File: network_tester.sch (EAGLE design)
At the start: 47 parts, among them SW1 SPST_TACT-KMR2, U1 Joystick, U2 RN2483, U3 ATSAMD21G-A, U5 MCP1640, X1 GPS, X2 868, X3 32.768, X4 microUSB, X5 434

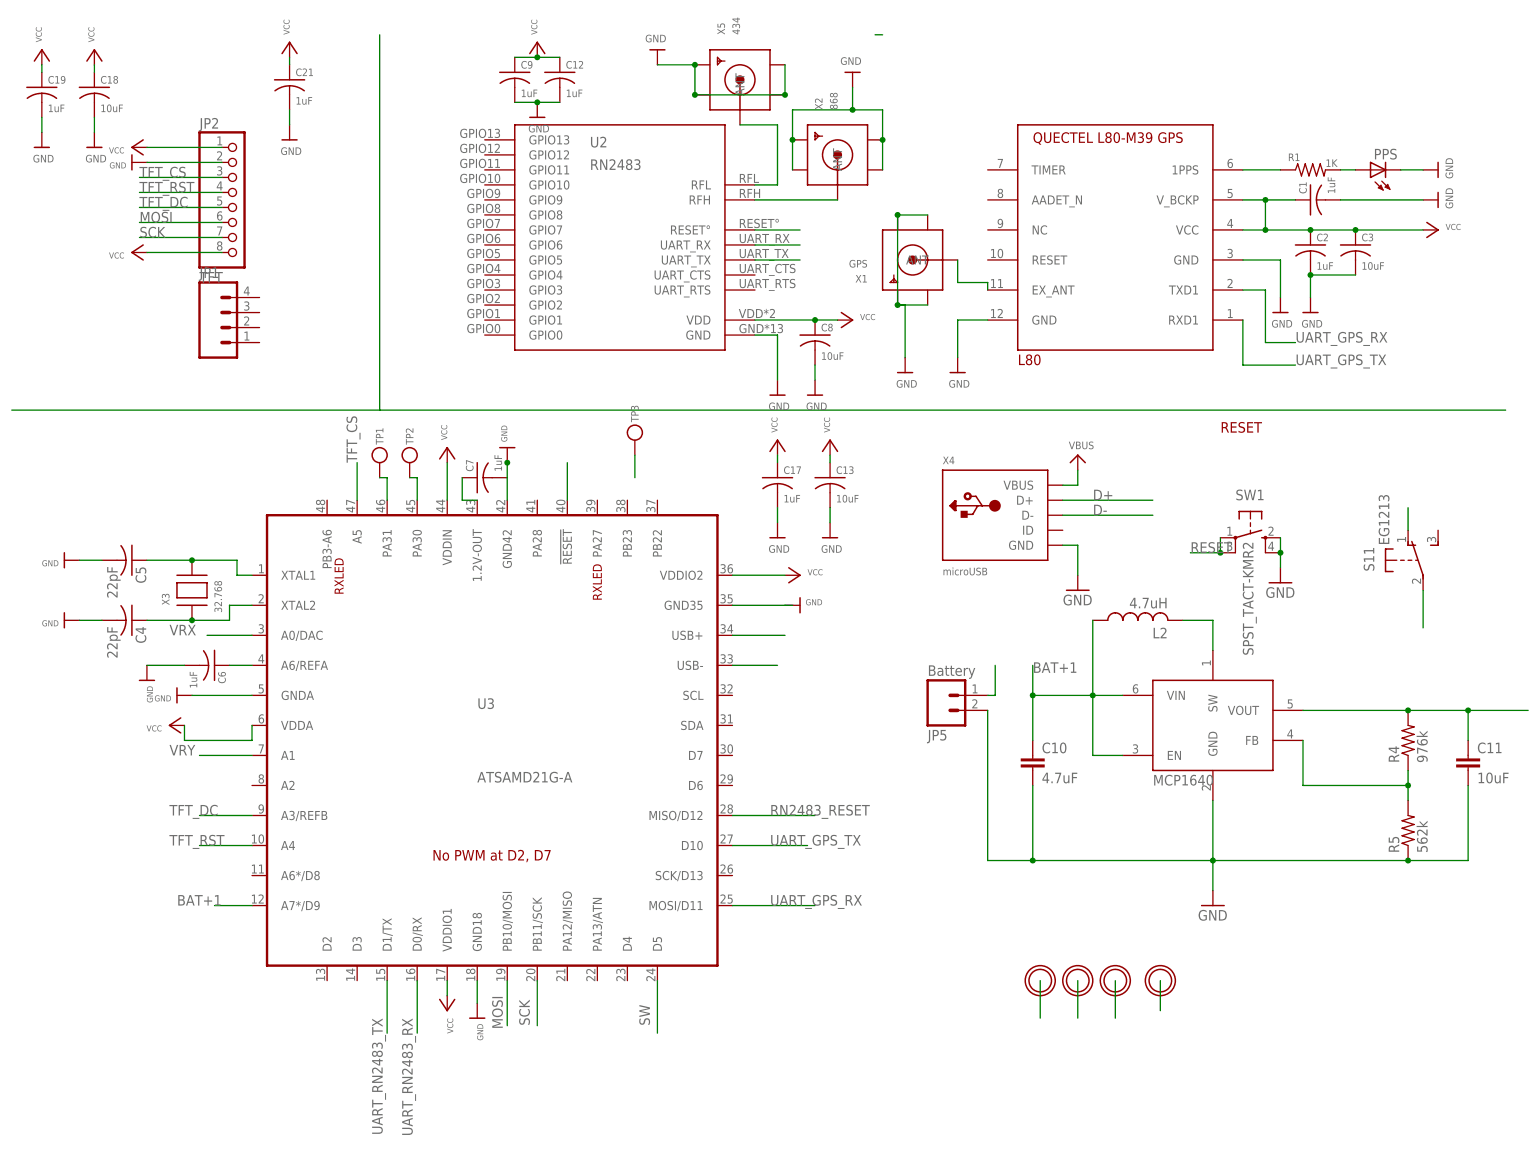
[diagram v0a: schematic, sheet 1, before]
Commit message: Test points added, fixed board labels
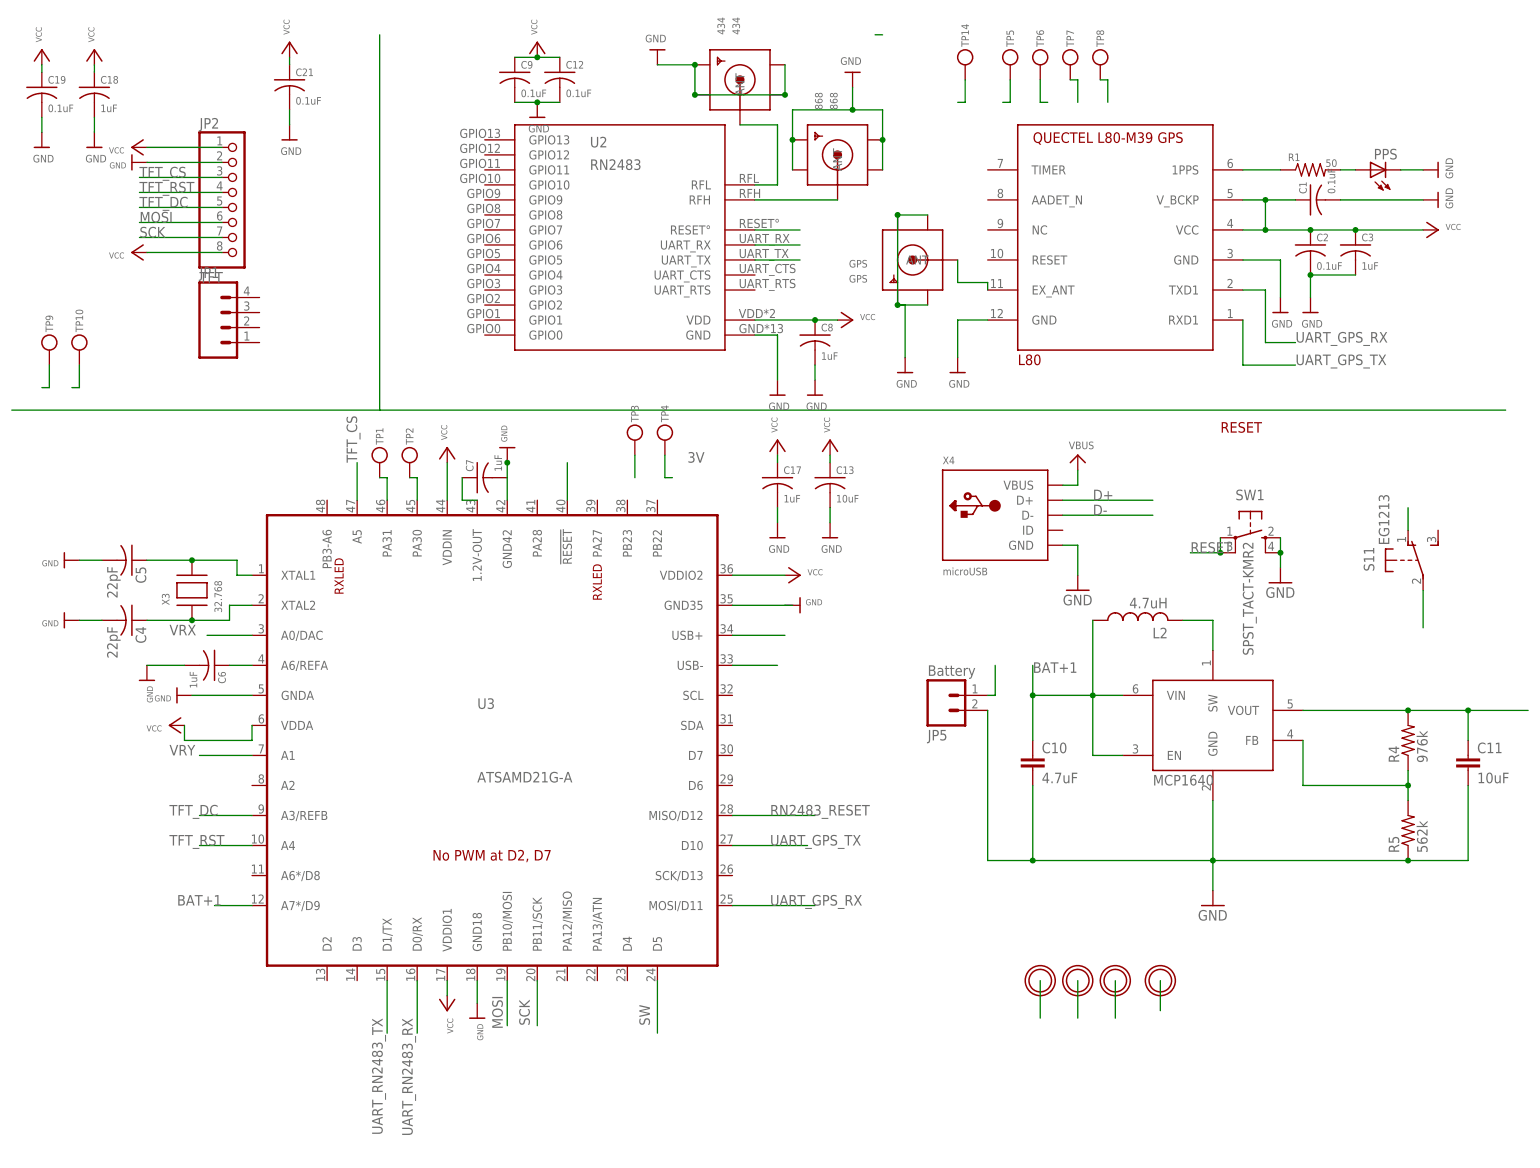
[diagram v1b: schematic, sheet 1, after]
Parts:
- added TP10, TP14, TP4, TP5, TP6, TP7, TP8, TP9: (no value), Adafruit Feather M0 Basic rev C:TESTPOINTROUND1.5MM
- C1, C12, C14, C15, C19, C2, C21, C9: value 1uF -> 0.1uF
- C16, C18, C3, C8: value 10uF -> 1uF
- R1: value 1K -> 50
- renumbered X1 to GPS, X2 to 868, X5 to 434
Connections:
- net 3V: now also TP4.P$1
- net MOSI: now also TP9.P$1
- net RN2483_RESET: now also TP14.P$1
- net SCK: now also TP10.P$1
- net UART_GPS_RX: now also TP7.P$1
- net UART_GPS_TX: now also TP8.P$1
- net UART_RN2483_RX: now also TP6.P$1
- net UART_RN2483_TX: now also TP5.P$1

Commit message: test point resolved
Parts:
- removed TP10, TP14, TP5, TP6, TP7, TP8, TP9: (no value), Adafruit Feather M0 Basic rev C:TESTPOINTROUND1.5MM
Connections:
- net MOSI: no longer TP9.P$1
- net RN2483_RESET: no longer TP14.P$1
- net SCK: no longer TP10.P$1
- net UART_GPS_RX: no longer TP7.P$1
- net UART_GPS_TX: no longer TP8.P$1
- net UART_RN2483_RX: no longer TP6.P$1
- net UART_RN2483_TX: no longer TP5.P$1

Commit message: First commit of board for external fabbing -- untested
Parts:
- removed PPS: (no value), adafruit:LEDCHIPLED_0805
- removed SW1: SPST_TACT-KMR2, adafruit:SPST_TACT-KMR2
- removed X3: 32.768, Adafruit Feather M0 Basic rev C:XTAL-3.2X1.5
- added C20, C22, C23: 100nf, Seeed-Capacitor:CERAMIC-100NF-25V-10%-X7R(0402)
- added D1: RED-0805, Seeed-LED:SMD-LED-CLEAR-RED(0805)
- added SW2: DHT-4235A, Seeed-Switch:SMD-BUTTON-TOP-DHT-4235A(4P-4.2X3.2MM)
- added Y1: 32.768, Seeed-Crystal Oscillator:SMD-CRYSTAL-32.768KHZ-12.5PF-20PPM-90K(2P-L2.0X1.2MM)
- C1, C12, C14, C15, C19, C2, C21, C9: value 0.1uF -> 100nf; device adafruit:C-USC0603 -> Seeed-Capacitor:CERAMIC-100NF-25V-10%-X7R(0402)
- C10: value 4.7uF -> 4.7uf; device SparkFun:CAP0805 -> Seeed-Capacitor:CERAMIC-4.7UF-6.3V-20%-X5R(0402)
- C11: value 10uF -> 10uf; device SparkFun:CAP0805 -> Seeed-Capacitor:CERAMIC-10UF-6.3V-20%-X5R(0402)
- C13: value 10uF -> 10uf; device adafruit:C-USC0805 -> Seeed-Capacitor:CERAMIC-10UF-6.3V-20%-X5R(0402)
- C16: value 1uF -> 1UF; device adafruit:C-USC0805 -> Seeed-Capacitor:CERAMIC-1UF-6.3V-10%-X5R(0402)
- C17, C7: value 1uF -> 1UF; device adafruit:C-USC0603 -> Seeed-Capacitor:CERAMIC-1UF-6.3V-10%-X5R(0402)
- C18, C3, C8: value 1uF -> 1UF 6.3V; device adafruit:C-USC0805 -> Seeed-Capacitor:CERAMIC-1UF-6.3V-10%-X5R(0402)
- C4, C5: value 22pF -> 22pf; device adafruit:C-USC0603 -> Seeed-Capacitor:CERAMIC-22PF-50V-5%-NPO(0402)
- C6: value 1uF -> 1UF 6.3V; device adafruit:C-USC0603 -> Seeed-Capacitor:CERAMIC-1UF-6.3V-10%-X5R(0402)
- U3: value ATSAMD21G-A -> ATSAMD21G-M; device Albert-Arduino:ATSAMD21G-A -> Albert-Arduino:ATSAMD21G-M
- X4: value microUSB -> ZX62-B-5PA; device microbuilder:USB_MICRO_20329_V2 -> Seeed-Connector:MICRO-USB-SMD(ZX62-B-5PA)
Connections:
- net 3V: now also C20.2, C22.1, C23.1
- net GND: now also C20.1, C22.2, C23.2, C7.2, D1.-, SW2.B1, X4.SHIELD; no longer PPS.C, SW1.S, SW1.S1
- net N$2: now also D1.+; no longer PPS.A
- net N$3: now also Y1.1; no longer X3.P$1
- net N$7: now also Y1.2; no longer X3.P$2
- net RESET: now also SW2.A0; no longer SW1.P, SW1.P1
